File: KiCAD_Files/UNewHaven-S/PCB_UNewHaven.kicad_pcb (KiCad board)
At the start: 2 copper layers, 73.7 x 48.3 mm, 28 parts, among them J1 Conn_01x15_Female, J2 Conn_01x15_Female, SW1 SW_Push, SW2 SW_Push, SW3 SW_Push, U2 LM35-LP

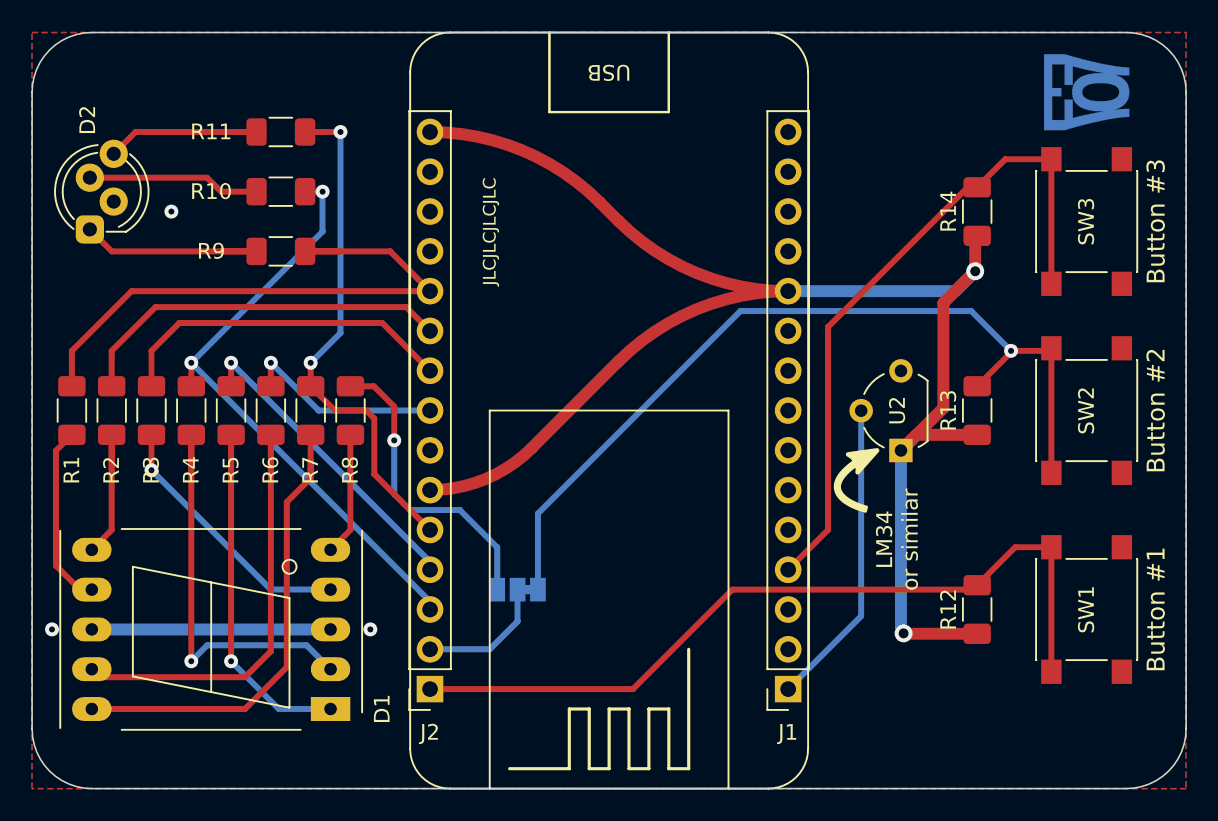
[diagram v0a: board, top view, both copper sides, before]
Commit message: UNewHaven Version 1.2 Update. Removed project from pre-release in README.md
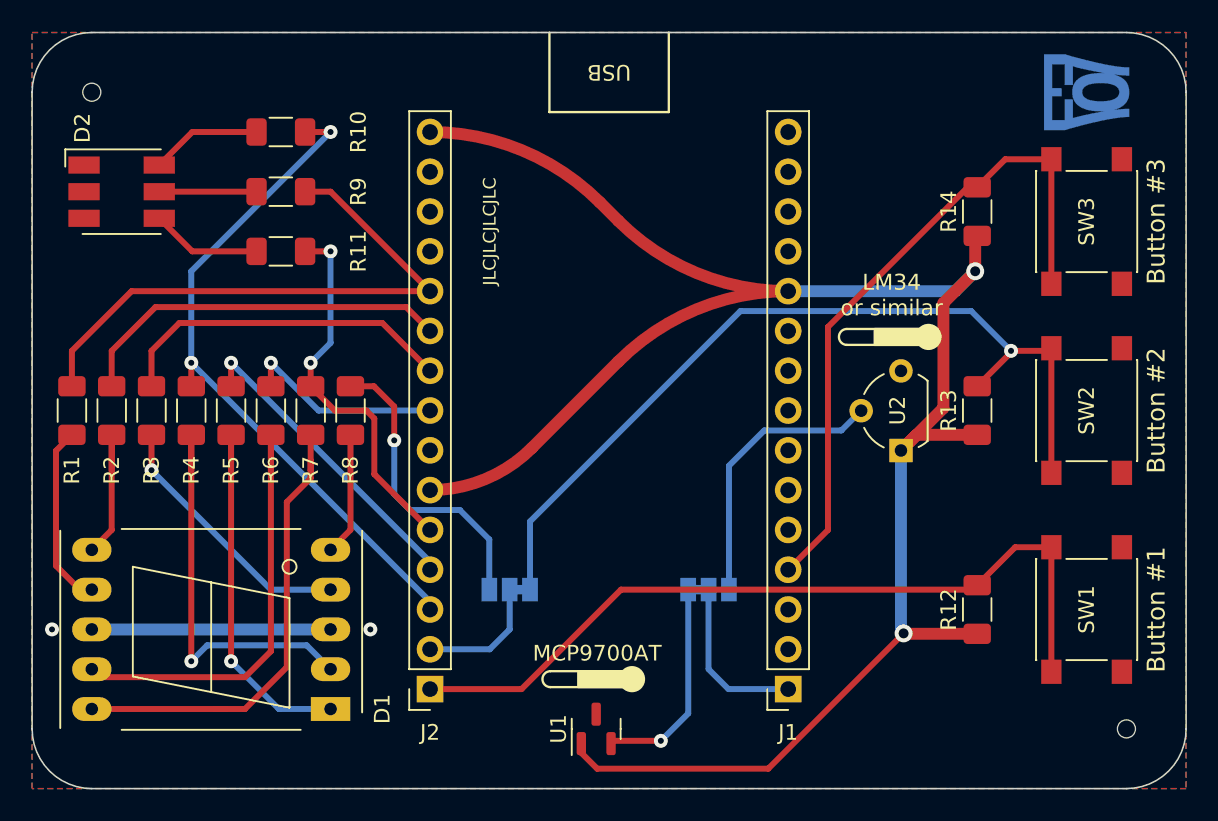
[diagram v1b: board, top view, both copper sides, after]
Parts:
- removed the REF** at (189.2, 51.4)
- added JP2: SolderJumper_3_Bridged12, Jumper:SolderJumper-3_P1.3mm_Bridged12_Pad1.0x1.5mm, B.Cu at (208.3, 62.9)
- added REF**: JLC_Assembly_Tooling, CustomFootprints:JLC_Assembly_Tooling, F.Cu at (168.9, 31.1)
- added REF**: JLC_Assembly_Tooling, CustomFootprints:JLC_Assembly_Tooling, F.Cu at (234.9, 71.8)
- added U1: MCP9700AT-ETT, Package_TO_SOT_SMD:SOT-23, F.Cu at (201.1, 71.8)
- D2: value LED_RKGB -> LED_RGB; footprint LED_THT:LED_D5.0mm-4_RGB_Staggered_Pins -> LED_SMD:LED_RGB_5050-6
- R1, R10, R11, R2, R3, R4, R5, R6, R7, R8, R9: value 1k -> 330
- moved R11 7.62 mm to (181.0, 41.3)
- moved R10 3.81 mm to (181.0, 33.7)
- moved R9 3.81 mm to (181.0, 37.5)
- moved D2 3.15 mm to (170.8, 37.5), turned to 0 degrees
- moved JP1 0.51 mm to (195.6, 62.9)
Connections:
- D2 pad 1: Net-(D2-Pad1) -> GND
- D2 pad 3: Net-(D2-Pad3) -> GND
- R10 pad 2: Net-(D2-Pad3) -> Net-(D2-Pad6)
- R9 pad 2: Net-(D2-Pad1) -> Net-(D2-Pad5)
- U2 pad 2: /TEMP -> Net-(JP2-Pad3)
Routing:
- net +3V3: track 102.5 -> 127.6 mm
- net Net-(JP2-Pad3): track 0.00 -> 17.8 mm
- net Net-(JP2-Pad1): track 0.00 -> 13.6 mm, vias 0 -> 1
- net Net-(D2-Pad1): track 13.5 -> 0.00 mm
- net Net-(D2-Pad3): track 11.0 -> 0.00 mm
- net /TEMP: track 19.7 -> 10.7 mm
- net /SEGG: track 32.8 -> 24.3 mm
- net Net-(D2-Pad6): track 0.00 -> 7.08 mm
- net Net-(D2-Pad5): track 0.00 -> 6.21 mm
- net Net-(D2-Pad4): track 12.0 -> 7.08 mm
- net /SEGD: track 39.1 -> 43.6 mm
- net /SEGA: track 38.0 -> 37.3 mm
- net GND: vias 3 -> 2
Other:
- board text added: "Basic NodeMCU Development Board V1.2 UNewHaven Edition"
- board text added: "MCP9700AT"
- board text removed: "Basic NodeMCU Development Board V1.1S"

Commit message: Almost finished Rev1.3 of the UNewHaven board
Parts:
- removed REF** (x2): JLC_Assembly_Tooling, CustomFootprints:JLC_Assembly_Tooling
- added BZ1: Buzzer, Buzzer_Beeper:Buzzer_12x9.5RM7.6, B.Cu at (198.4, 38.7)
- added R15: 1k, Resistor_SMD:R_1206_3216Metric_Pad1.30x1.75mm_HandSolder, F.Cu at (195.6, 48.9)
- added SW-T1: SW_Push_DPDT, Button_Switch_THT:SW_CuK_JS202011CQN_DPDT_Straight, F.Cu at (223.8, 66.6)
- added SW-T2: SW_Push_DPDT, Button_Switch_THT:SW_CuK_JS202011CQN_DPDT_Straight, F.Cu at (223.8, 53.9)
- added SW-T3: SW_Push_DPDT, Button_Switch_THT:SW_CuK_JS202011CQN_DPDT_Straight, F.Cu at (223.8, 41.9)
- moved R12 27.6 mm to (198.8, 57.1), turned to -90 degrees
- moved R14 27.4 mm to (205.1, 57.1), turned to -90 degrees
- moved R13 23.6 mm to (201.9, 54.0), turned to -90 degrees
- moved U2 0.63 mm to (219.9, 54.0)
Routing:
- net +3V3: track 127.6 -> 147.5 mm, vias 2 -> 3
- net /BT3: track 43.2 -> 55.7 mm
- net Net-(R15-Pad1): track 0.00 -> 9.67 mm
- net /SEGDP: track 19.4 -> 28.7 mm
- net /BT1: track 51.4 -> 58.9 mm
- net /BT2: track 55.4 -> 62.4 mm
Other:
- board text added: "Basic NodeMCU Development Board V1.3 UNewHaven Edition"
- board text removed: "Basic NodeMCU Development Board V1.2 UNewHaven Edition"

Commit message: Added some external pin headers
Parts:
- added J3: Conn_01x01_Female, CustomFootprints:SingleExternalWire, F.Cu at (211.5, 29.8)
- added J4: Conn_01x01_Female, CustomFootprints:SingleExternalWire, F.Cu at (191.8, 29.8)
- added J5: Conn_01x01_Female, CustomFootprints:SingleExternalWire, F.Cu at (196.2, 29.8)
- added J6: Conn_01x01_Female, CustomFootprints:SingleExternalWire, F.Cu at (207.6, 29.8)
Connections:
- J1 pad 15: unconnected-(J1-Pad15) -> /VIN
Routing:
- net /TEMP: track 10.7 -> 45.5 mm, vias 0 -> 2
- net /IO-C1: track 8.15 -> 41.4 mm
- net /VIN: track 0.00 -> 4.60 mm
- net +3V3: track 147.5 -> 146.3 mm
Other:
- board text added: "+"
- board text added: "-"
- board text added: "ADC0"
- board text added: "D1"

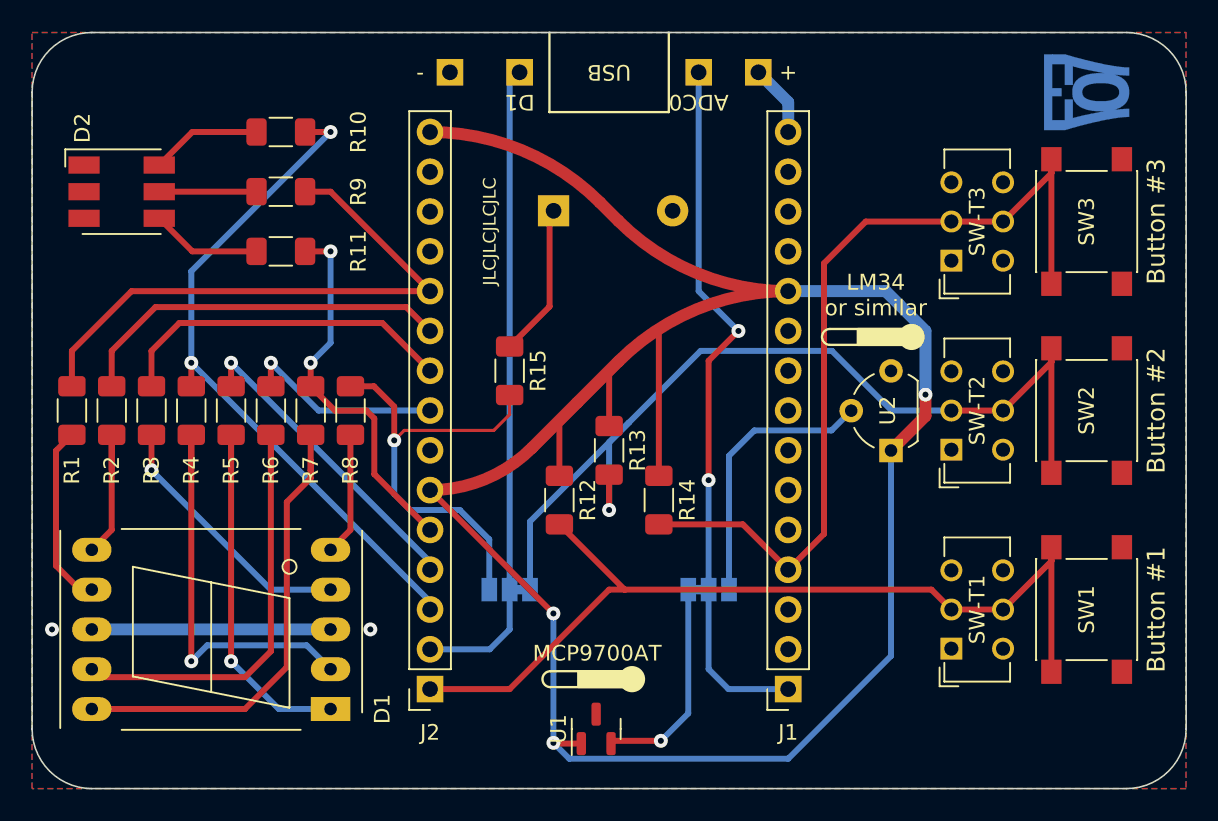
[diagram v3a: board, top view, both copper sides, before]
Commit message: Changed the external pinout's connectors. Minor silk changes. DRC fixes
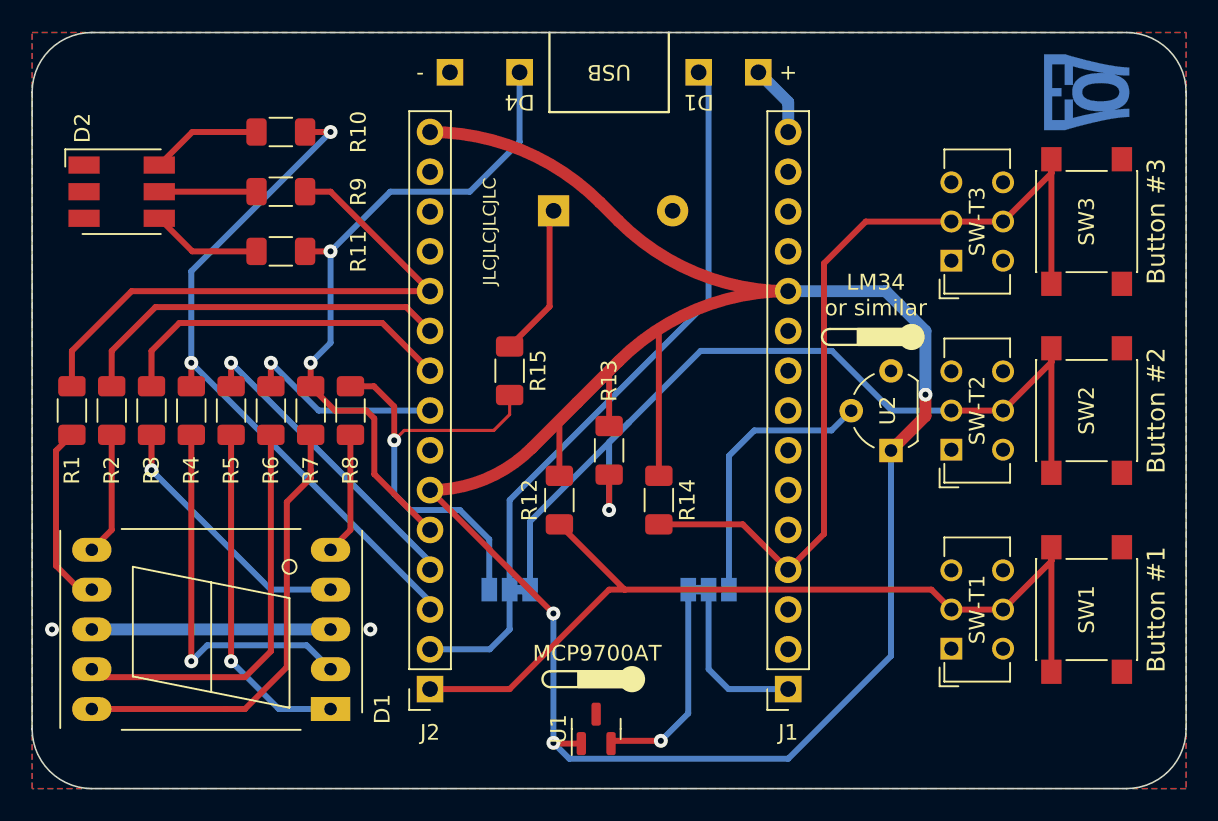
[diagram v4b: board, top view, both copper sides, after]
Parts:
- moved J5 11.4 mm to (207.6, 29.8)
- moved J6 11.4 mm to (196.2, 29.8)
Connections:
- J6 pad 1: /TEMP -> /SEGG
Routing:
- net /TEMP: track 45.5 -> 10.7 mm, vias 2 -> 0
- net /SEGG: track 24.3 -> 43.7 mm
- net /IO-C1: track 41.4 -> 46.7 mm
- net Net-(D1-Pad9): track 28.4 -> 26.1 mm
- net Net-(D1-Pad6): track 10.1 -> 7.87 mm
- net Net-(D1-Pad2): track 26.7 -> 24.4 mm
- net Net-(D1-Pad1): track 24.3 -> 22.1 mm
- net Net-(D1-Pad10): track 30.3 -> 29.0 mm
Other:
- board text added: "Concept by Mark Morton W1MEM Designed by Jamal Bouajjaj (Electro707) ~~B.S.E.E Class of 2022~~"
- board text added: "D4"
- board text removed: "ADC0"
- board text removed: "Concept by Mark Morton W1MEM Designed by Jamal Bouajjaj (B.S.E.E Class of 2022)"
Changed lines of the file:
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@@
   (net 47 "unconnected-(SW-T3-Pad3)")
   (footprint "CustomFootprints:SingleExternalWire" (layer "F.Cu")
-    (at 196.215 29.845)
+    (at 207.645 29.845)
     (descr "Through hole straight socket strip, 1x01, 2.54mm pitch, single row (from Kicad 4.0.7), script generated")
     (tags "Through hole socket strip THT 1x01 2.54mm single row")
@@
     (property "Sheetname" "")
     (attr smd)
-    (fp_text reference "R12" (at 0 -1.82 90) (layer "F.SilkS")
+    (fp_text reference "R12" (at 0 1.905 90) (layer "F.SilkS")
       (effects (font (size 1 1) (thickness 0.15)))
     )
@@
     (property "Sheetname" "")
     (attr smd)
-    (fp_text reference "R13" (at 0 -1.82 90) (layer "F.SilkS")
+    (fp_text reference "R13" (at -4.445 0 90) (layer "F.SilkS")
       (effects (font (size 1 1) (thickness 0.15)))
     )
@@
   )
   (footprint "CustomFootprints:SingleExternalWire" (layer "F.Cu")
-    (at 207.645 29.845)
+    (at 196.215 29.845)
     (descr "Through hole straight socket strip, 1x01, 2.54mm pitch, single row (from Kicad 4.0.7), script generated")
     (tags "Through hole socket strip THT 1x01 2.54mm single row")
@@
     (fp_line (start 1.27 1.27) (end -1.27 1.27) (layer "F.Fab") (width 0.1))
     (pad "1" thru_hole rect (at 0 0) (size 1.7 1.7) (drill 1) (layers *.Cu *.Mask)
-      (net 22 "/TEMP") (pinfunction "Pin_1") (pintype "passive"))
+      (net 5 "/SEGG") (pinfunction "Pin_1") (pintype "passive"))
   )
   (footprint "Resistor_SMD:R_1206_3216Metric_Pad1.30x1.75mm_HandSolder" (layer "F.Cu")
@@
       (effects (font (size 1 1) (thickness 0.15)) (justify mirror))
     )
-    (fp_text user "+" (at -0.01 2.54 180) (layer "B.SilkS")
-      (effects (font (size 1 1) (thickness 0.15)) (justify mirror))
-    )
     (fp_text user "+" (at -0.01 2.54 180) (layer "B.Fab")
       (effects (font (size 1 1) (thickness 0.15)) (justify mirror))
@@
     (effects (font (size 2.54 2.54) (thickness 0.508)) (justify mirror))
   )
-  (gr_text "Concept by Mark Morton W1MEM\n\nDesigned by Jamal Bouajjaj \n(B.S.E.E Class of 2022)" (at 177.165 51.435 90) (layer "B.SilkS")
+  (gr_text "Concept by Mark Morton W1MEM\n\nDesigned by Jamal Bouajjaj (Electro707)\n~~B.S.E.E Class of 2022~~" (at 177.165 51.435 90) (layer "B.SilkS")
     (effects (font (size 1.016 1.016) (thickness 0.1524) italic) (justify mirror))
   )
@@
     (effects (font (size 0.8128 0.8128) (thickness 0.1524)))
   )
-  (gr_text "ADC0" (at 207.645 31.75 180) (layer "F.SilkS")
+  (gr_text "D1" (at 207.645 31.75 180) (layer "F.SilkS")
     (effects (font (size 1 1) (thickness 0.15)))
   )
@@
     (effects (font (size 1.143 1.143) (thickness 0.1778)))
   )
-  (gr_text "D1" (at 196.215 31.75 180) (layer "F.SilkS")
+  (gr_text "D4" (at 196.215 31.75 180) (layer "F.SilkS")
     (effects (font (size 1 1) (thickness 0.15)))
   )
@@
   (segment (start 219.9225 67.0975) (end 219.9225 53.985) (width 0.381) (layer "B.Cu") (net 2))
   (segment (start 201.93 55.525) (end 201.93 57.785) (width 0.381) (layer "F.Cu") (net 3))
-  (segment (start 229.995 47.625) (end 230.16 47.46) (width 0.381) (layer "F.Cu") (net 3))
   (segment (start 223.775 51.435) (end 227.075 51.435) (width 0.381) (layer "F.Cu") (net 3))
   (segment (start 230.16 48.35) (end 230.16 47.46) (width 0.381) (layer "F.Cu") (net 3))
@@
   (via (at 184.15 41.275) (size 0.889) (drill 0.381) (layers "F.Cu" "B.Cu") (net 5))
   (via (at 182.88 48.387) (size 0.889) (drill 0.381) (layers "F.Cu" "B.Cu") (net 5))
+  (segment (start 187.96 37.465) (end 184.15 41.275) (width 0.381) (layer "B.Cu") (net 5))
+  (segment (start 196.215 34.29) (end 193.04 37.465) (width 0.381) (layer "B.Cu") (net 5))
   (segment (start 184.15 47.117) (end 182.88 48.387) (width 0.381) (layer "B.Cu") (net 5))
   (segment (start 184.15 41.275) (end 184.15 47.117) (width 0.381) (layer "B.Cu") (net 5))
+  (segment (start 193.04 37.465) (end 187.96 37.465) (width 0.381) (layer "B.Cu") (net 5))
+  (segment (start 196.215 29.845) (end 196.215 34.29) (width 0.381) (layer "B.Cu") (net 5))
   (segment (start 180.34 49.885) (end 180.34 48.387) (width 0.381) (layer "F.Cu") (net 6))
   (via (at 180.34 48.387) (size 0.889) (drill 0.381) (layers "F.Cu" "B.Cu") (net 6))
@@
   (segment (start 168.91 65.405) (end 184.15 65.405) (width 0.762) (layer "B.Cu") (net 12))
   (segment (start 175.26 67.437) (end 175.26 52.985) (width 0.381) (layer "F.Cu") (net 13))
-  (segment (start 175.26 55.245) (end 175.26 52.985) (width 0.381) (layer "F.Cu") (net 13))
   (via (at 175.26 67.437) (size 0.889) (drill 0.381) (layers "F.Cu" "B.Cu") (net 13))
   (segment (start 184.15 67.945) (end 182.626 66.421) (width 0.381) (layer "B.Cu") (net 13))
@@
   (segment (start 185.42 59.055) (end 184.15 60.325) (width 0.381) (layer "F.Cu") (net 21))
   (segment (start 185.42 52.985) (end 185.42 59.055) (width 0.381) (layer "F.Cu") (net 21))
-  (segment (start 208.28 48.26) (end 208.28 55.88) (width 0.381) (layer "F.Cu") (net 22))
-  (segment (start 210.185 46.355) (end 208.28 48.26) (width 0.381) (layer "F.Cu") (net 22))
-  (via (at 210.185 46.355) (size 0.889) (drill 0.381) (layers "F.Cu" "B.Cu") (net 22))
-  (via (at 208.28 55.88) (size 0.889) (drill 0.381) (layers "F.Cu" "B.Cu") (net 22))
   (segment (start 208.28 62.865) (end 208.28 67.945) (width 0.381) (layer "B.Cu") (net 22))
-  (segment (start 208.28 55.88) (end 208.28 62.865) (width 0.381) (layer "B.Cu") (net 22))
   (segment (start 208.28 67.945) (end 209.55 69.215) (width 0.381) (layer "B.Cu") (net 22))
   (segment (start 209.55 69.215) (end 213.36 69.215) (width 0.381) (layer "B.Cu") (net 22))
-  (segment (start 207.645 29.845) (end 207.645 43.815) (width 0.381) (layer "B.Cu") (net 22))
-  (segment (start 207.645 43.815) (end 210.185 46.355) (width 0.381) (layer "B.Cu") (net 22))
-  (segment (start 177.8 55.245) (end 177.8 52.985) (width 0.381) (layer "F.Cu") (net 23))
   (segment (start 177.8 67.437) (end 177.8 52.985) (width 0.381) (layer "F.Cu") (net 23))
   (via (at 177.8 67.437) (size 0.889) (drill 0.381) (layers "F.Cu" "B.Cu") (net 23))
   (segment (start 184.15 70.485) (end 180.848 70.485) (width 0.381) (layer "B.Cu") (net 23))
   (segment (start 180.848 70.485) (end 177.8 67.437) (width 0.381) (layer "B.Cu") (net 23))
-  (segment (start 180.34 55.245) (end 180.34 52.985) (width 0.381) (layer "F.Cu") (net 27))
   (segment (start 169.418 68.453) (end 178.689 68.453) (width 0.381) (layer "F.Cu") (net 27))
   (segment (start 168.91 67.945) (end 169.418 68.453) (width 0.381) (layer "F.Cu") (net 27))
   (segment (start 178.689 68.453) (end 180.34 66.802) (width 0.381) (layer "F.Cu") (net 27))
   (segment (start 180.34 66.802) (end 180.34 52.985) (width 0.381) (layer "F.Cu") (net 27))
-  (segment (start 177.453554 70.485) (end 176.784 70.485) (width 0.381) (layer "F.Cu") (net 28))
-  (segment (start 182.88 55.245) (end 182.88 54.61) (width 0.381) (layer "F.Cu") (net 28))
   (segment (start 181.356 57.277) (end 182.88 55.753) (width 0.381) (layer "F.Cu") (net 28))
   (segment (start 177.453554 70.485) (end 178.689 70.485) (width 0.381) (layer "F.Cu") (net 28))
@@
   (segment (start 166.624 61.341) (end 168.148 62.865) (width 0.381) (layer "F.Cu") (net 35))
   (segment (start 166.624 54.001) (end 166.624 61.341) (width 0.381) (layer "F.Cu") (net 35))
-  (segment (start 170.18 55.245) (end 170.18 52.985) (width 0.381) (layer "F.Cu") (net 36))
   (segment (start 168.91 60.325) (end 170.18 59.055) (width 0.381) (layer "F.Cu") (net 36))
   (segment (start 170.18 59.055) (end 170.18 52.985) (width 0.381) (layer "F.Cu") (net 36))
@@
   (segment (start 194.28 59.66) (end 194.28 62.865) (width 0.381) (layer "B.Cu") (net 37))
   (segment (start 188.214 56.769) (end 188.214 53.34) (width 0.381) (layer "B.Cu") (net 37))
+  (segment (start 208.28 44.45) (end 195.58 57.15) (width 0.381) (layer "B.Cu") (net 38))
+  (segment (start 208.28 30.48) (end 208.28 44.45) (width 0.381) (layer "B.Cu") (net 38))
   (segment (start 194.31 66.675) (end 190.5 66.675) (width 0.381) (layer "B.Cu") (net 38))
-  (segment (start 196.215 29.845) (end 195.58 30.48) (width 0.381) (layer "B.Cu") (net 38))
+  (segment (start 207.645 29.845) (end 208.28 30.48) (width 0.381) (layer "B.Cu") (net 38))
   (segment (start 195.58 62.865) (end 195.58 65.405) (width 0.381) (layer "B.Cu") (net 38))
+  (segment (start 195.58 57.15) (end 195.58 62.865) (width 0.381) (layer "B.Cu") (net 38))
   (segment (start 195.58 65.405) (end 194.31 66.675) (width 0.381) (layer "B.Cu") (net 38))
-  (segment (start 195.58 30.48) (end 195.58 62.865) (width 0.381) (layer "B.Cu") (net 38))
   (segment (start 209.58 54.326) (end 211.201 52.705) (width 0.381) (layer "B.Cu") (net 39))
   (segment (start 209.58 62.865) (end 209.58 54.326) (width 0.381) (layer "B.Cu") (net 39))
